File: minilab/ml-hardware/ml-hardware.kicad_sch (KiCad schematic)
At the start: 12 parts, among them J1 Molex lite-trap, J10 Molex lite-trap, J11 Molex lite-trap, J12 Molex lite-trap, J13 Molex lite-trap, J2 Jack-DC, J4 Molex lite-trap, J5 Molex lite-trap, J6 Molex lite-trap, J7 Molex lite-trap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

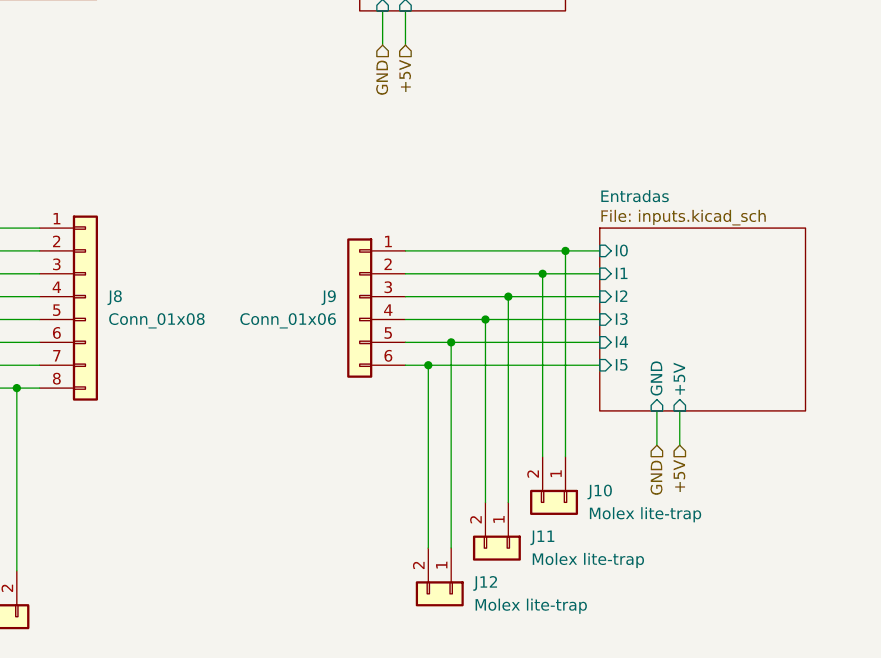
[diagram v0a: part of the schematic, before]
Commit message: minilab: change 4096 to 74HC540 for 1byte input
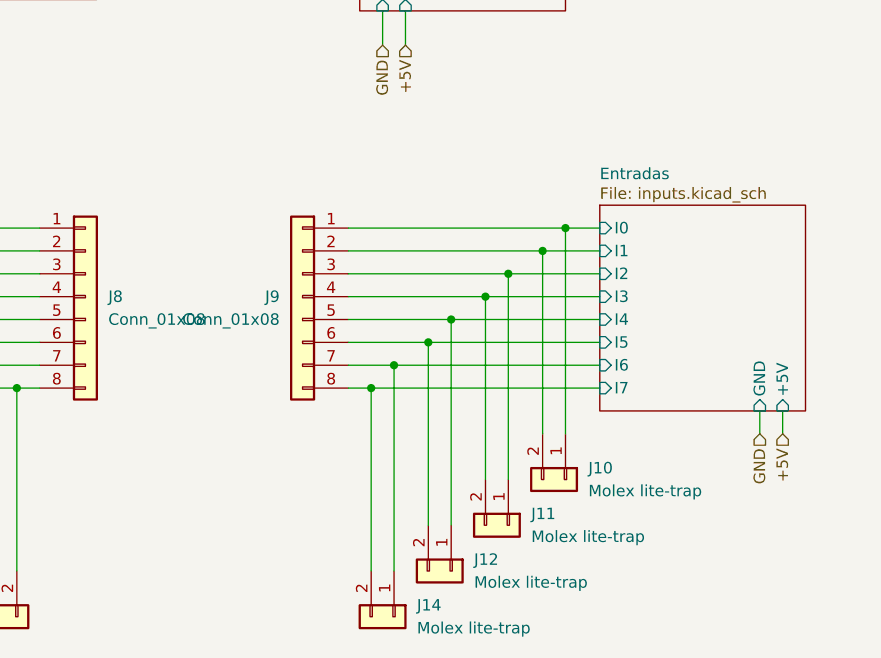
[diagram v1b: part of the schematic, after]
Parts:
- removed J9: Conn_01x06, symbol Connector_Generic:Conn_01x06
- added J14: Molex lite-trap, symbol Connector_Generic:Conn_01x02
- added J9: Conn_01x08, symbol Connector_Generic:Conn_01x08
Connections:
- net Entradas/I0: now also J9.1 (Pin_1)
- net Entradas/I1: now also J9.2 (Pin_2)
- net Entradas/I2: now also J9.3 (Pin_3)
- net Entradas/I3: now also J9.4 (Pin_4)
- net Entradas/I4: now also J9.5 (Pin_5)
- net Entradas/I5: now also J9.6 (Pin_6)
- new net Entradas/I6: J14.1 (Pin_1), J9.7 (Pin_7)
- new net Entradas/I7: J14.2 (Pin_2), J9.8 (Pin_8)
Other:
- sheet Entradas ports: added I6, I7; removed none

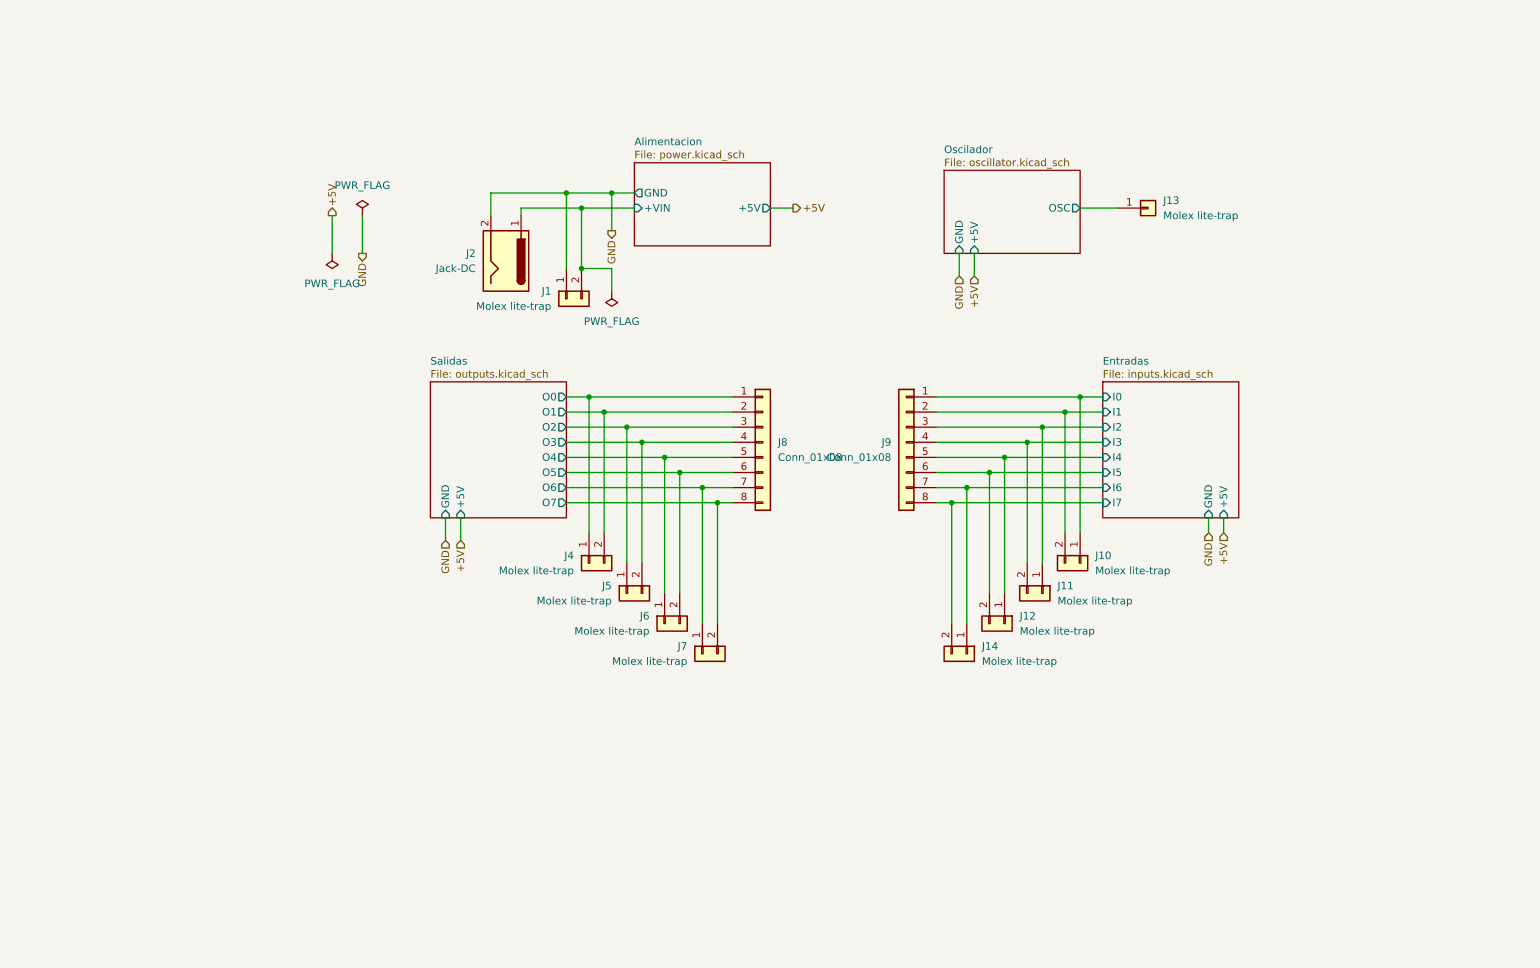
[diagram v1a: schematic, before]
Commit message: minilab: Enforce "pcb/page" hierarchy on schematic
This does not apply (necessarily) to subpages.
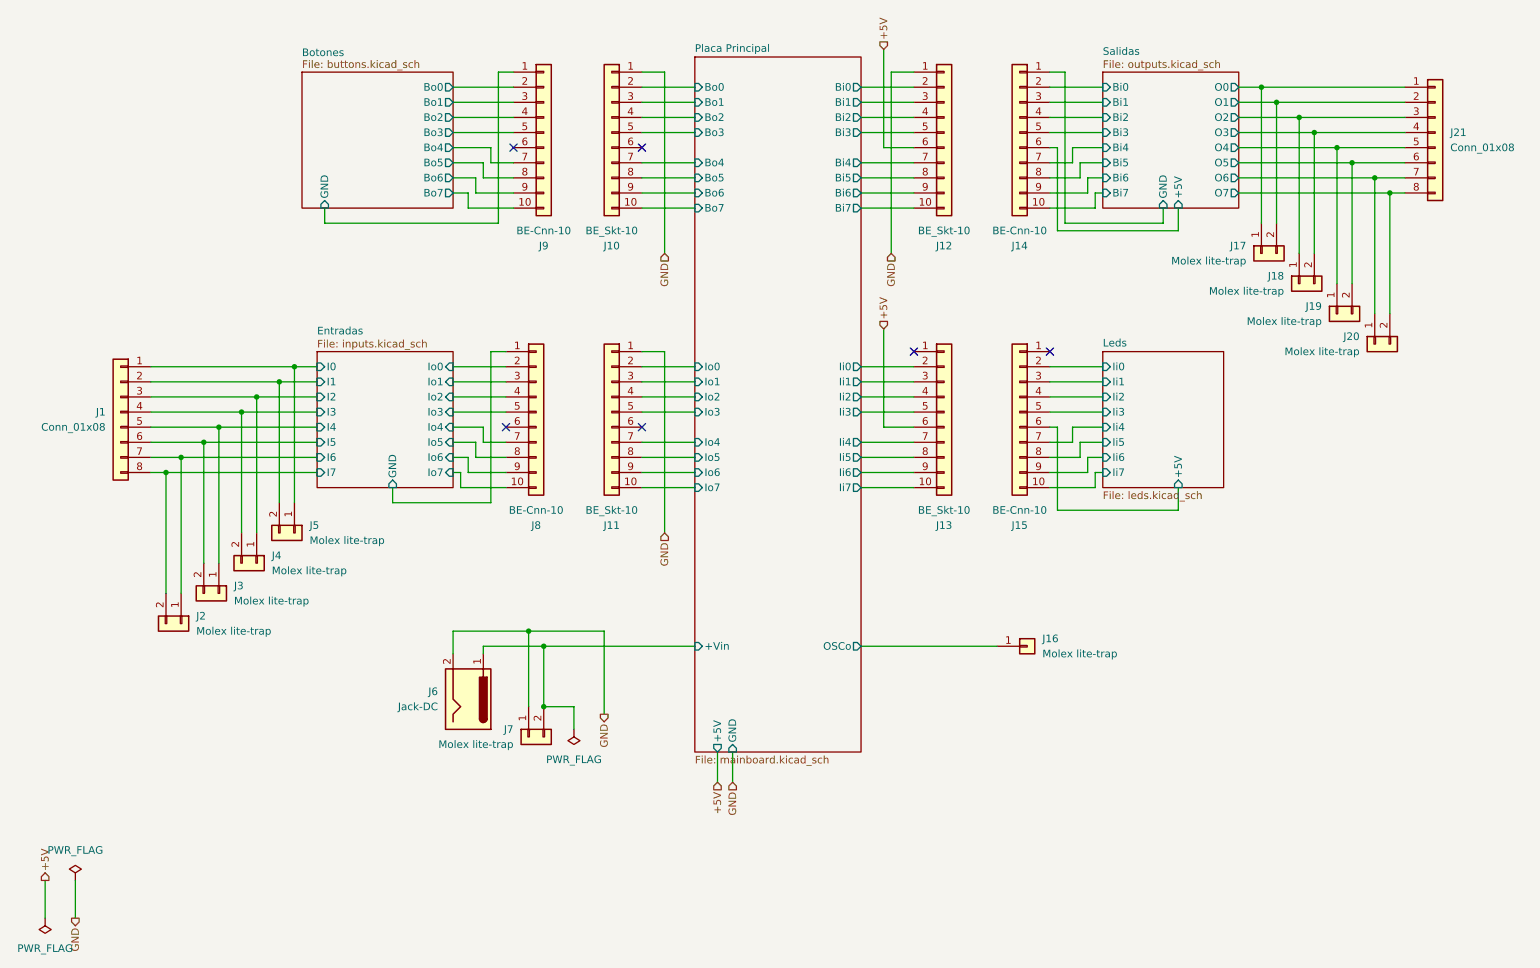
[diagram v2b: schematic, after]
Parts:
- added J10, J11, J12, J13: BE_Skt-10, Extras:EdgeSocket-10, symbol Connector_Generic:Conn_01x10
- added J14, J15, J8, J9: BE-Cnn-10, Extras:EdgeConn-10, symbol Connector_Generic:Conn_01x10
- J1: renamed from J9; footprint (none) -> Connector_PinSocket_2.54mm:PinSocket_1x08_P2.54mm_Horizontal
- J16: renamed from J13; footprint (none) -> Extras:104238-0210
- J17: renamed from J4; footprint (none) -> Extras:104238-0210
- J18: renamed from J5; footprint (none) -> Extras:104238-0210
- J19: renamed from J6; footprint (none) -> Extras:104238-0210
- J2: renamed from J14; footprint (none) -> Extras:104238-0210
- J20: renamed from J7; footprint (none) -> Extras:104238-0210
- J21: renamed from J8; footprint (none) -> Connector_PinSocket_2.54mm:PinSocket_1x08_P2.54mm_Horizontal
- J3: renamed from J12; footprint (none) -> Extras:104238-0210
- J4: renamed from J11; footprint (none) -> Extras:104238-0210
- J5: renamed from J10; footprint (none) -> Extras:104238-0210
- J6: renamed from J2; footprint (none) -> Connector_BarrelJack:BarrelJack_Horizontal
- J7: renamed from J1; footprint (none) -> Extras:104238-0210
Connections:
- net +5V: now also J12.6 (Pin_6), J13.6 (Pin_6)
- net GND: now also J10.1 (Pin_1), J11.1 (Pin_1), J12.1 (Pin_1)
- net Alimentacion/+VIN renamed Placa Principal/+Vin
- net Oscilador/OSC renamed Placa Principal/OSCo
- new net Botones/Bo0: J9.2 (Pin_2)
- new net Botones/Bo1: J9.3 (Pin_3)
- new net Botones/Bo2: J9.4 (Pin_4)
- new net Botones/Bo3: J9.5 (Pin_5)
- new net Botones/Bo4: J9.7 (Pin_7)
- new net Botones/Bo5: J9.8 (Pin_8)
- new net Botones/Bo6: J9.9 (Pin_9)
- new net Botones/Bo7: J9.10 (Pin_10)
- new net Botones/GND: J9.1 (Pin_1)
- new net Entradas/GND: J8.1 (Pin_1)
- new net Entradas/Io0: J8.2 (Pin_2)
- new net Entradas/Io1: J8.3 (Pin_3)
- new net Entradas/Io2: J8.4 (Pin_4)
- new net Entradas/Io3: J8.5 (Pin_5)
- new net Entradas/Io4: J8.7 (Pin_7)
- new net Entradas/Io5: J8.8 (Pin_8)
- new net Entradas/Io6: J8.9 (Pin_9)
- new net Entradas/Io7: J8.10 (Pin_10)
- new net Leds/+5V: J15.6 (Pin_6)
- new net Leds/Ii0: J15.2 (Pin_2)
- new net Leds/Ii1: J15.3 (Pin_3)
- new net Leds/Ii2: J15.4 (Pin_4)
- new net Leds/Ii3: J15.5 (Pin_5)
- new net Leds/Ii4: J15.7 (Pin_7)
- new net Leds/Ii5: J15.8 (Pin_8)
- new net Leds/Ii6: J15.9 (Pin_9)
- new net Leds/Ii7: J15.10 (Pin_10)
- new net Placa Principal/Bi0: J12.2 (Pin_2)
- new net Placa Principal/Bi1: J12.3 (Pin_3)
- new net Placa Principal/Bi2: J12.4 (Pin_4)
- new net Placa Principal/Bi3: J12.5 (Pin_5)
- new net Placa Principal/Bi4: J12.7 (Pin_7)
- new net Placa Principal/Bi5: J12.8 (Pin_8)
- new net Placa Principal/Bi6: J12.9 (Pin_9)
- new net Placa Principal/Bi7: J12.10 (Pin_10)
- new net Placa Principal/Bo0: J10.2 (Pin_2)
- new net Placa Principal/Bo1: J10.3 (Pin_3)
- new net Placa Principal/Bo2: J10.4 (Pin_4)
- new net Placa Principal/Bo3: J10.5 (Pin_5)
- new net Placa Principal/Bo4: J10.7 (Pin_7)
- new net Placa Principal/Bo5: J10.8 (Pin_8)
- new net Placa Principal/Bo6: J10.9 (Pin_9)
- new net Placa Principal/Bo7: J10.10 (Pin_10)
- new net Placa Principal/Ii0: J13.2 (Pin_2)
- new net Placa Principal/Ii1: J13.3 (Pin_3)
- new net Placa Principal/Ii2: J13.4 (Pin_4)
- new net Placa Principal/Ii3: J13.5 (Pin_5)
- new net Placa Principal/Ii4: J13.7 (Pin_7)
- new net Placa Principal/Ii5: J13.8 (Pin_8)
- new net Placa Principal/Ii6: J13.9 (Pin_9)
- new net Placa Principal/Ii7: J13.10 (Pin_10)
- new net Placa Principal/Io0: J11.2 (Pin_2)
- new net Placa Principal/Io1: J11.3 (Pin_3)
- new net Placa Principal/Io2: J11.4 (Pin_4)
- new net Placa Principal/Io3: J11.5 (Pin_5)
- new net Placa Principal/Io4: J11.7 (Pin_7)
- new net Placa Principal/Io5: J11.8 (Pin_8)
- new net Placa Principal/Io6: J11.9 (Pin_9)
- new net Placa Principal/Io7: J11.10 (Pin_10)
- new net Salidas/+5V: J14.6 (Pin_6)
- new net Salidas/Bi0: J14.2 (Pin_2)
- new net Salidas/Bi1: J14.3 (Pin_3)
- new net Salidas/Bi2: J14.4 (Pin_4)
- new net Salidas/Bi3: J14.5 (Pin_5)
- new net Salidas/Bi4: J14.7 (Pin_7)
- new net Salidas/Bi5: J14.8 (Pin_8)
- new net Salidas/Bi6: J14.9 (Pin_9)
- new net Salidas/Bi7: J14.10 (Pin_10)
- new net Salidas/GND: J14.1 (Pin_1)
- no-connect marks 0 -> 6
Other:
- removed sheet Alimentacion
- removed sheet Oscilador
- added sheet Botones (buttons.kicad_sch)
- added sheet Leds (leds.kicad_sch)
- added sheet Placa Principal (mainboard.kicad_sch)
- sheet Entradas ports: added Io0, Io1, Io2, Io3, Io4, Io5, Io6, Io7; removed +5V
- sheet Salidas ports: added Bi0, Bi1, Bi2, Bi3, Bi4, Bi5, Bi6, Bi7; removed none
- moved on the sheet: J1, J16, J17, J18, J19, J2, J20, J21, J3, J4, J5, J6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

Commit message: minilab: cambia jerarquia y agrega pcb
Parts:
- removed J16: Molex lite-trap, Extras:104238-0210, symbol Connector_Generic:Conn_01x01
- removed J6: Jack-DC, Connector_BarrelJack:BarrelJack_Horizontal, symbol Connector:Jack-DC
- removed J7: Molex lite-trap, Extras:104238-0210, symbol Connector_Generic:Conn_01x02
- added J16: Molex lite-trap, Extras:104238-0210, symbol Connector_Generic:Conn_01x02
- added J23: BE_Skt-2_1, Extras:EdgeSocket-2, symbol Connector_Generic:Conn_01x02
- added J24: BE_Cnn-2_1, Extras:EdgeConn-2, symbol Connector_Generic:Conn_01x02
- J10: value BE_Skt-10 -> WF-0.1; footprint Extras:EdgeSocket-10 -> Connector_Molex:Molex_KK-254_AE-6410-09A_1x09_P2.54mm_Vertical; symbol Connector_Generic:Conn_01x10 -> Connector_Generic:Conn_01x09
- J11: value BE_Skt-10 -> BE_Skt-10_3
- J12: value BE_Skt-10 -> BE_Skt-10_1
- J13: value BE_Skt-10 -> BE_Skt-10_2
- J14: value BE-Cnn-10 -> BE-Cnn-10_1
- J15: value BE-Cnn-10 -> BE-Cnn-10_2
- J8: value BE-Cnn-10 -> BE-Cnn-10_3
- J9: value BE-Cnn-10 -> WF-0.1; footprint Extras:EdgeConn-10 -> Connector_Molex:Molex_KK-254_AE-6410-09A_1x09_P2.54mm_Vertical; symbol Connector_Generic:Conn_01x10 -> Connector_Generic:Conn_01x09
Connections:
- net Botones/Bo4: now also J9.6 (Pin_6); no longer J9.7 (Pin_7)
- net Botones/Bo5: now also J9.7 (Pin_7); no longer J9.8 (Pin_8)
- net Botones/Bo6: now also J9.8 (Pin_8); no longer J9.9 (Pin_9)
- net Botones/Bo7: now also J9.9 (Pin_9); no longer J9.10 (Pin_10)
- net GND: now also J23.1 (Pin_1)
- net Placa Principal/+Vin: now also J23.2 (Pin_2)
- net Placa Principal/Bo4: now also J10.6 (Pin_6); no longer J10.7 (Pin_7)
- net Placa Principal/Bo5: now also J10.7 (Pin_7); no longer J10.8 (Pin_8)
- net Placa Principal/Bo6: now also J10.8 (Pin_8); no longer J10.9 (Pin_9)
- net Placa Principal/Bo7: now also J10.9 (Pin_9); no longer J10.10 (Pin_10)
- net Placa Principal/OSCo: now also J16.1 (Pin_1), J16.2 (Pin_2)
- new net Entrada alimentacion/+Vin: J24.2 (Pin_2)
- new net Entrada alimentacion/GND: J24.1 (Pin_1)
- no-connect marks 6 -> 4
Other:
- added sheet Entrada alimentacion (power_in.kicad_sch)
